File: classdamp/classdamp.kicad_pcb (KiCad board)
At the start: 2 copper layers, 22 parts

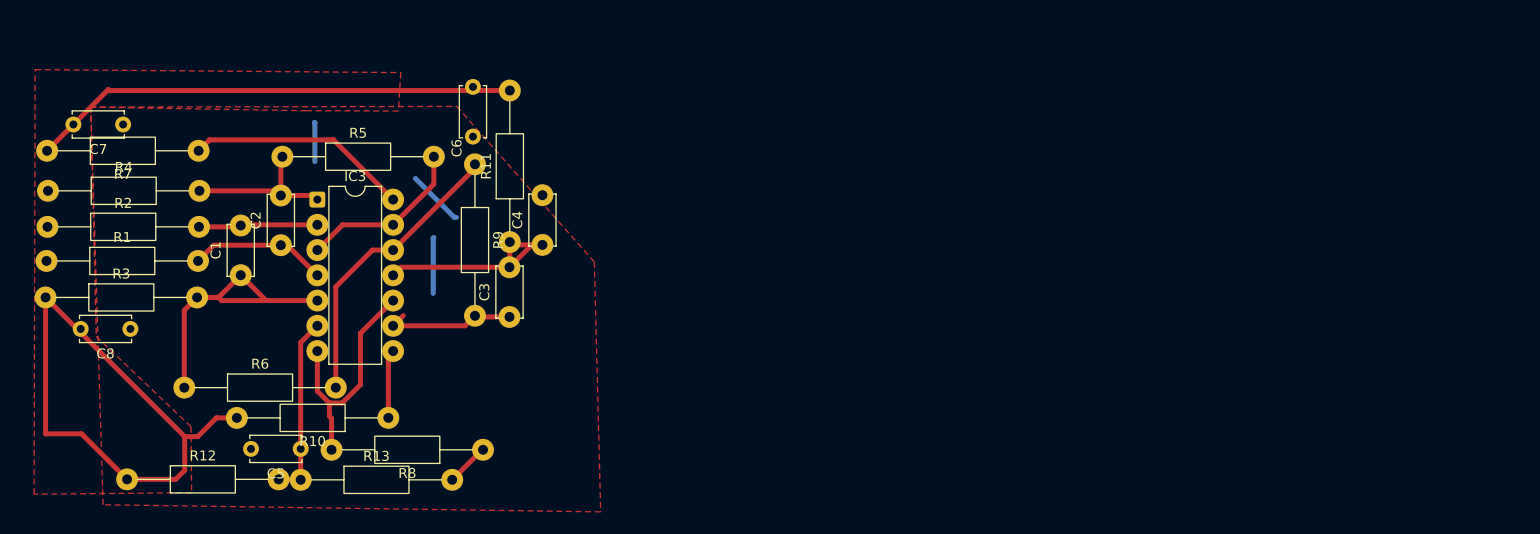
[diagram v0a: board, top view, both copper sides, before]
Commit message: Comparator stage
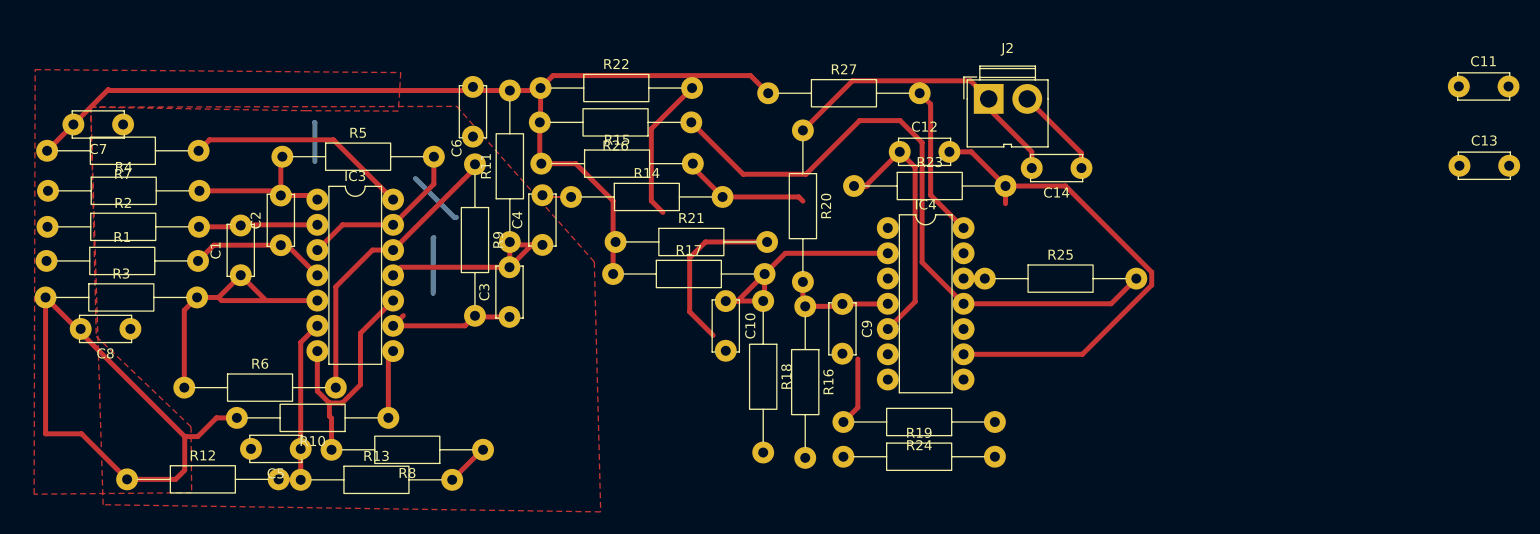
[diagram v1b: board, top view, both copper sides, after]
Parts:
- added C10: 1n, Capacitor_THT:C_Disc_D5.0mm_W2.5mm_P5.00mm, F.Cu at (143.8, 88.0)
- added C11: 1n, Capacitor_THT:C_Disc_D5.0mm_W2.5mm_P5.00mm, F.Cu at (217.5, 66.4)
- added C12: 1n, Capacitor_THT:C_Disc_D5.0mm_W2.5mm_P5.00mm, F.Cu at (161.3, 73.0)
- added C13: 1n, Capacitor_THT:C_Disc_D5.0mm_W2.5mm_P5.00mm, F.Cu at (217.6, 74.4)
- added C14: 1n, Capacitor_THT:C_Disc_D5.0mm_W2.5mm_P5.00mm, F.Cu at (179.5, 74.6)
- added C9: 1n, Capacitor_THT:C_Disc_D5.0mm_W2.5mm_P5.00mm, F.Cu at (155.5, 88.3)
- added IC4: ~, Package_DIP:DIP-14_W7.62mm, F.Cu at (160.1, 80.6)
- added J2: Conn_01x02_Pin, Connector:JWT_A3963_1x02_P3.96mm_Vertical, F.Cu at (170.2, 67.6)
- added R14: 1k, Resistor_THT:R_Axial_DIN0207_L6.3mm_D2.5mm_P15.24mm_Horizontal, F.Cu at (128.2, 77.5)
- added R15: 5k, Resistor_THT:R_Axial_DIN0207_L6.3mm_D2.5mm_P15.24mm_Horizontal, F.Cu at (125.2, 74.1)
- added R16: 5k, Resistor_THT:R_Axial_DIN0207_L6.3mm_D2.5mm_P15.24mm_Horizontal, F.Cu at (151.8, 88.5)
- added R17: 5k, Resistor_THT:R_Axial_DIN0207_L6.3mm_D2.5mm_P15.24mm_Horizontal, F.Cu at (132.4, 85.2)
- added R18: 5k, Resistor_THT:R_Axial_DIN0207_L6.3mm_D2.5mm_P15.24mm_Horizontal, F.Cu at (147.5, 88.0)
- added R19: 1k, Resistor_THT:R_Axial_DIN0207_L6.3mm_D2.5mm_P15.24mm_Horizontal, F.Cu at (155.6, 103.6)
- added R20: 1k, Resistor_THT:R_Axial_DIN0207_L6.3mm_D2.5mm_P15.24mm_Horizontal, F.Cu at (151.5, 70.8)
- added R21: 1k, Resistor_THT:R_Axial_DIN0207_L6.3mm_D2.5mm_P15.24mm_Horizontal, F.Cu at (132.7, 82.0)
- added R22: 1k, Resistor_THT:R_Axial_DIN0207_L6.3mm_D2.5mm_P15.24mm_Horizontal, F.Cu at (125.1, 66.5)
- added R23: 6.7k, Resistor_THT:R_Axial_DIN0207_L6.3mm_D2.5mm_P15.24mm_Horizontal, F.Cu at (156.7, 76.4)
- added R24: 620, Resistor_THT:R_Axial_DIN0207_L6.3mm_D2.5mm_P15.24mm_Horizontal, F.Cu at (170.8, 100.1)
- added R25: 10k, Resistor_THT:R_Axial_DIN0207_L6.3mm_D2.5mm_P15.24mm_Horizontal, F.Cu at (169.8, 85.7)
- added R26: 1k, Resistor_THT:R_Axial_DIN0207_L6.3mm_D2.5mm_P15.24mm_Horizontal, F.Cu at (140.3, 70.0)
- added R27: 1k, Resistor_THT:R_Axial_DIN0207_L6.3mm_D2.5mm_P15.24mm_Horizontal, F.Cu at (148.0, 67.1)
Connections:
- C4 pad 2: unconnected-(C4-Pad2) -> Net-(C4-Pad2)
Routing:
- net Net-(IC4-Q4_C): track 0.00 -> 64.9 mm
- net Net-(IC4-Q2_C): track 0.00 -> 52.1 mm
- net +12V: track 108.3 -> 159.5 mm
- net Net-(IC4-Q4_B): track 0.00 -> 50.2 mm
- net Net-(J2-Pin_1): track 0.00 -> 30.3 mm
- net Net-(IC4-Q1_B): track 0.00 -> 24.8 mm
- net Net-(IC4-Q2_B): track 0.00 -> 23.8 mm
- net Net-(IC4-Q5_C): track 0.00 -> 15.4 mm
- net Net-(IC4-Q1_C): track 0.00 -> 14.7 mm
- net GND: track 21.6 -> 30.8 mm
- net Net-(C4-Pad2): track 0.00 -> 3.21 mm
- net Net-(IC4-Q5_B): track 0.00 -> 2.14 mm

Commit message: Low power side done
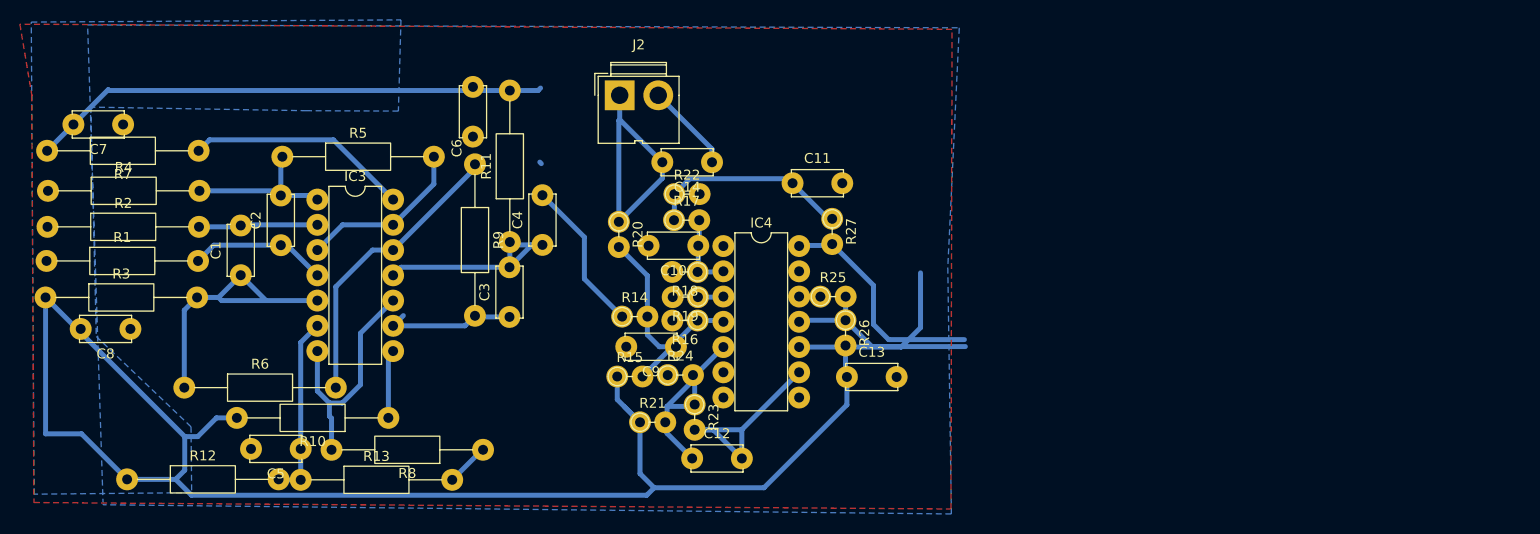
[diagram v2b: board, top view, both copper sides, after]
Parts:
- R14, R15, R16, R17, R18, R19, R20, R21, R22, R23, R24, R25, R26, R27: footprint Resistor_THT:R_Axial_DIN0207_L6.3mm_D2.5mm_P15.24mm_Horizontal -> Resistor_THT:R_Axial_DIN0204_L3.6mm_D1.6mm_P2.54mm_Vertical
- moved C11 67.7 mm to (150.5, 76.1)
- moved C13 65.2 mm to (156.0, 95.6)
- moved C12 37.2 mm to (140.4, 103.8)
- moved C14 37.2 mm to (142.4, 74.0)
- moved J2 37.1 mm to (133.1, 67.3)
- moved R24 33.2 mm to (137.9, 95.4), turned to 0 degrees
- moved R23 27.2 mm to (140.6, 98.4), turned to -90 degrees
- moved R26 25.2 mm to (155.8, 89.9), turned to -90 degrees
- moved R15 22.7 mm to (132.9, 95.6)
- moved R19 21.7 mm to (141.0, 87.6), turned to 180 degrees
- moved R20 20.7 mm to (133.0, 80.0)
- moved R21 18.3 mm to (135.1, 100.2)
- moved C9 17.3 mm to (138.8, 92.6), turned to 180 degrees
- moved R22 17.2 mm to (138.6, 77.2)
- moved R25 16.6 mm to (153.3, 87.5)
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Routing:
- net +12V: track 159.5 -> 224.3 mm
- net Net-(IC4-Q4_C): track 64.9 -> 20.3 mm
- net Net-(IC4-Q2_C): track 52.1 -> 20.6 mm
- net Net-(IC4-Q4_B): track 50.2 -> 21.7 mm
- net GND: track 30.8 -> 49.5 mm
- net Net-(IC4-Q1_B): track 24.8 -> 7.90 mm
- net (no net): track 15.3 -> 0.00 mm
- net Net-(IC4-Q1_C): track 14.7 -> 0.00 mm
- net Net-(C4-Pad2): track 3.21 -> 15.8 mm
- net Net-(IC4-Q5_C): track 15.4 -> 22.2 mm
- net Net-(J2-Pin_1): track 30.3 -> 26.6 mm
- net Net-(IC4-Q1_Q2_E): track 0.00 -> 2.58 mm
- added copper zone on B.Cu, net +12V
- added copper zone on B.Cu, net GND
- removed copper zone on F.Cu, net +12V
